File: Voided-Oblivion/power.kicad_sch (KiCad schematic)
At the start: 133 parts, among them Q1 AO3401, Q10 BC847B, Q11 BC847B, Q13 NCE4009S, Q14 NCE4009S, Q2 AO4407A, Q3 BC857, Q4 AO4407A, Q5 AO4407A, Q6 AO4407A, Q7 AO4407A, Q8 BC847B, Q9 BC847B, U10 TLV431BQDBZR, U11 LM2903, U12 AP2171WG-7, U13 TPD2E2U06DRL, U14 TPD2E2U06DRL, U15 LM66100DCKT, U16 AP2171WG-7, U17 LM74700QDDF, U18 LM74700QDDF, U2 TS3USB30ERSWR, U5 TPS54302, U6 TPS54302, U7 TLV76733DRVR, U9 LM66100DCKT

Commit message: pcb almooost done
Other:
- note added: "BS+: Bootstrap rail(5V) PD+: Power Delivery rail (9-20V) +5VA: 5V Analog/clean 5V +5VP: 5V Power/Noisy 5V (for rgb) SM+: Sub-Module power (5V) VBUS: Combined power from both USB-C ports (after ideal diodes)"
- note removed: "BS+: Bootstrap rail(5V) PD+: Power Delivery rail (9-20V) +5VA: 5V Analog/clean 5V +5VP: 5V Power/Noisy 5V (for rgb) SM+: Sub-Module power (5V)"
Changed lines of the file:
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@@
 		)
 	)
-	(text "BS+: Bootstrap rail(5V)\nPD+: Power Delivery rail (9-20V)\n+5VA: 5V Analog/clean 5V\n+5VP: 5V Power/Noisy 5V (for rgb)\nSM+: Sub-Module power (5V)"
+	(text "BS+: Bootstrap rail(5V)\nPD+: Power Delivery rail (9-20V)\n+5VA: 5V Analog/clean 5V\n+5VP: 5V Power/Noisy 5V (for rgb)\nSM+: Sub-Module power (5V)\nVBUS: Combined power from both USB-C ports (after ideal diodes)"
 		(exclude_from_sim no)
 		(at 16.51 274.32 0)

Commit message: THE PCB IS FINAWWYY (electricaly) DONE YAAAAAAAAAAAAAA :33333 ^w^ >w<
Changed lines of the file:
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@@
 	)
 	(junction
+		(at 372.11 157.48)
+		(diameter 0)
+		(color 0 0 0 0)
+	)
+	(junction
 		(at 83.82 77.47)
 		(diameter 0)
@@
 	)
 	(junction
+		(at 251.46 162.56)
+		(diameter 0)
+		(color 0 0 0 0)
+	)
+	(junction
 		(at 88.9 179.07)
 		(diameter 0)
@@
 	)
 	(symbol
+		(lib_id "power:PWR_FLAG")
+		(at 372.11 157.48 270)
+		(unit 1)
+		(body_style 1)
+		(exclude_from_sim no)
+		(in_bom yes)
+		(on_board yes)
+		(in_pos_files yes)
+		(dnp no)
+		(fields_autoplaced yes)
+		(property "Reference" "#FLG012"
+			(at 374.015 157.48 0)
+			(hide yes)
+			(show_name no)
+			(do_not_autoplace no)
+			(effects
+				(font
+					(size 1.27 1.27)
+				)
+			)
+		)
+		(property "Value" "PWR_FLAG"
+			(at 375.92 157.4799 90)
+			(show_name no)
+			(do_not_autoplace no)
+			(effects
+				(font
+					(size 1.27 1.27)
+				)
+				(justify left)
+			)
+		)
+		(property "Footprint" ""
+			(at 372.11 157.48 0)
+			(hide yes)
+			(show_name no)
+			(do_not_autoplace no)
+			(effects
+				(font
+					(size 1.27 1.27)
+				)
+			)
+		)
+		(property "Datasheet" ""
+			(at 372.11 157.48 0)
+			(hide yes)
+			(show_name no)
+			(do_not_autoplace no)
+			(effects
+				(font
+					(size 1.27 1.27)
+				)
+			)
+		)
+		(property "Description" "Special symbol for telling ERC where power comes from"
+			(at 372.11 157.48 0)
+			(hide yes)
+			(show_name no)
+			(do_not_autoplace no)
+			(effects
+				(font
+					(size 1.27 1.27)
+				)
+			)
+		)
+		(pin "1"
+		)
+		(instances
+			(project "Voided-Oblivion"
+				(path "/d39297fe-343b-4cf0-9c31-a16e101c76da/889be6bb-77c0-4884-a2da-d27e1f17090a"
+					(reference "#FLG012")
+					(unit 1)
+				)
+			)
+		)
+	)
+	(symbol
 		(lib_id "Device:R")
 		(at 123.19 246.38 180)
@@
 					(unit 1)
 				)
+			)
+		)
+	)
+	(symbol
+		(lib_id "power:PWR_FLAG")
+		(at 251.46 162.56 90)
+		(unit 1)
+		(body_style 1)
+		(exclude_from_sim no)
+		(in_bom yes)
+		(on_board yes)
+		(in_pos_files yes)
+		(dnp no)
+		(fields_autoplaced yes)
+		(property "Reference" "#FLG011"
+			(at 249.555 162.56 0)
+			(hide yes)
+			(show_name no)
+			(do_not_autoplace no)
+			(effects
+				(font
+					(size 1.27 1.27)
+				)
+			)
+		)
+		(property "Value" "PWR_FLAG"
+			(at 247.65 162.5599 90)
+			(show_name no)
+			(do_not_autoplace no)
+			(effects
+				(font
+					(size 1.27 1.27)
+				)
+				(justify left)
+			)
+		)
+		(property "Footprint" ""
+			(at 251.46 162.56 0)
+			(hide yes)
+			(show_name no)
+			(do_not_autoplace no)
+			(effects
+				(font
+					(size 1.27 1.27)
+				)
+			)
+		)
+		(property "Datasheet" ""
+			(at 251.46 162.56 0)
+			(hide yes)
+			(show_name no)
+			(do_not_autoplace no)
+			(effects
+				(font
+					(size 1.27 1.27)
+				)
+			)
+		)
+		(property "Description" "Special symbol for telling ERC where power comes from"
+			(at 251.46 162.56 0)
+			(hide yes)
+			(show_name no)
+			(do_not_autoplace no)
+			(effects
+				(font
+					(size 1.27 1.27)
+				)
+			)
+		)
+		(pin "1"
+		)
+		(instances
+			(project "Voided-Oblivion"
+				(path "/d39297fe-343b-4cf0-9c31-a16e101c76da/889be6bb-77c0-4884-a2da-d27e1f17090a"
+					(reference "#FLG011")
+					(unit 1)
+				)

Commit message: small changes
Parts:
- C114, C115, C116, C117, C118, C119, C120, C127, C128, C129, C130, C23, C24, C25, C27, C30, C32, C33, C36, C37, C38, C39, C41, C42, C43, C44, C45, C76: footprint Capacitor_SMD:C_0402_1005Metric -> Voided-Oblivion-misc:C_0402_1005Metric-no-silkscreen-text
- R102, R103, R12, R14, R15, R16, R18, R19, R20, R21, R22, R24, R25, R26, R27, R28, R29, R32, R33, R34, R35, R37, R38, R39, R40, R41, R42, R43, R44, R45, R46, R47, R48, R49, R50, R51, R67, R68, R69, R70, R71, R72, R73, R74, R75, R76, R77, R78, R79, R80, R81, R82, R83, R92, R95, R96: footprint Resistor_SMD:R_0402_1005Metric -> Voided-Oblivion-misc:R_0402_1005Metric-no-silkscreen-text
- R30: footprint Resistor_SMD:R_0402_1005Metric -> Voided-Oblivion-misc:R_0402_1005Metric-no-silkscreen-text; MPN ARG02BTC4422 -> ARG02BTC3572
- R31: footprint Resistor_SMD:R_0402_1005Metric -> Voided-Oblivion-misc:R_0402_1005Metric-no-silkscreen-text; MPN (none) -> ARG02BTC1002
- R36: value 10kΩ -> 1kΩ; footprint Resistor_SMD:R_0402_1005Metric -> Voided-Oblivion-misc:R_0402_1005Metric-no-silkscreen-text; LCSC C25744 -> C11702; MPN 0402WGF1002TCE -> 0402WGF1001TCE
- U10: symbol Reference_Voltage:TL431DBZ -> Voided-Oblivion-misc:TL431BQDBZ
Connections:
- net +1V24ref: now also U10.2 (K); no longer U10.1 (K)
- net VBUS1: now also R37.1
- net VBUS2: no longer R37.1
- net at R27.1, R28.2: now also U10.1 (REF); no longer U10.2 (REF)
- net at Q3.3 (C): now also R36.2; no longer R36.1
- net at C45.1, D5.1 (A), Q1.1 (G)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: now also R36.1; no longer R36.2
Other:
- moved on the sheet: C39, D3, R37

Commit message: i think everything but silk is acctualy done this time for reals
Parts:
- R38: value 100kΩ -> 4.7kΩ; LCSC C25741 -> C25900; MPN 0402WGF1003TCE -> 0402WGF4701TCE
- R79, R80, R81, R82: value 100kΩ -> 2.2kΩ; LCSC C25741 -> (none); MPN 0402WGF1003TCE -> (none); Manufacturer UNI-ROYAL(Uniroyal Elec) -> (none)

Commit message: BOMB update  (ignore the "B" on the end of that first word, it has no significant meaning) and some library linking
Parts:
- C121, C40, C77: LCSC C315248 -> C89632; MPN CL05A106MP5NUNC -> CL31B106KBHNNNE
- C26, C31: LCSC (none) -> C89632; MPN (none) -> CL31B106KBHNNNE; Manufacturer (none) -> Samsung Electro-Mechanics
- C28, C29, C34, C35: LCSC (none) -> C12891; MPN (none) -> CL31A226KAHNNNE; Manufacturer (none) -> Samsung Electro-Mechanics
- Q13, Q14: MPN (none) -> NCE4009S; Manufacturer (none) -> Wuxi NCE Power Semiconductor
- R22: MPN (none) -> 0402WGF5101TCE; Manufacturer (none) -> UNI-ROYAL(Uniroyal Elec)
- R31: Manufacturer (none) -> Viking Tech
- R75, R76, R77, R78: value 10kΩ -> 4.7kΩ; LCSC C25744 -> C25900; MPN 0402WGF1002TCE -> 0402WGF4701TCE
- R79, R80, R81, R82: LCSC (none) -> C25879; MPN (none) -> 0402WGF2201TCE; Manufacturer (none) -> UNI-ROYAL(Uniroyal Elec)
- U10: MPN (none) -> TLV431BQDBZR; Manufacturer (none) -> Texas Instruments
- U17, U18: MPN (none) -> LM74700QDDFRQ1; Manufacturer (none) -> Texas Instruments
- USB1, USB2: MPN (none) -> HC-TYPE-C-16P-01A; Manufacturer (none) -> HCTL

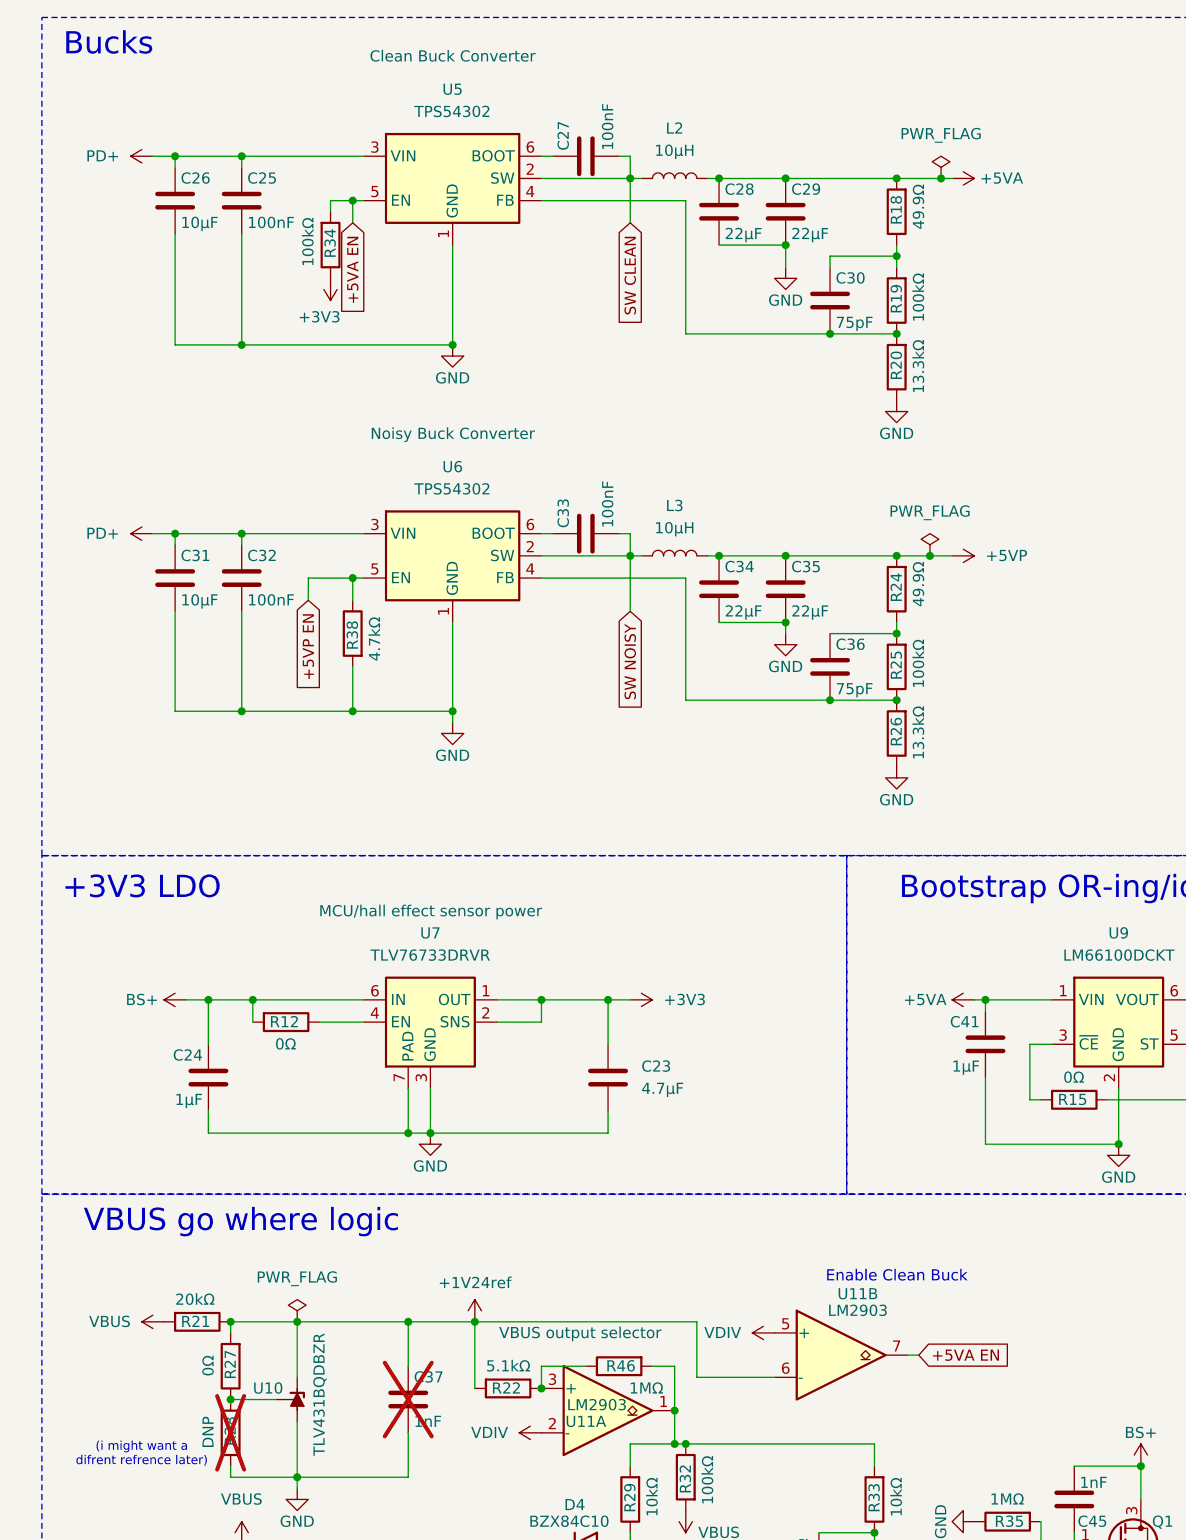
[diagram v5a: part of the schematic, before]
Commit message: change thing to vbus instead of pd
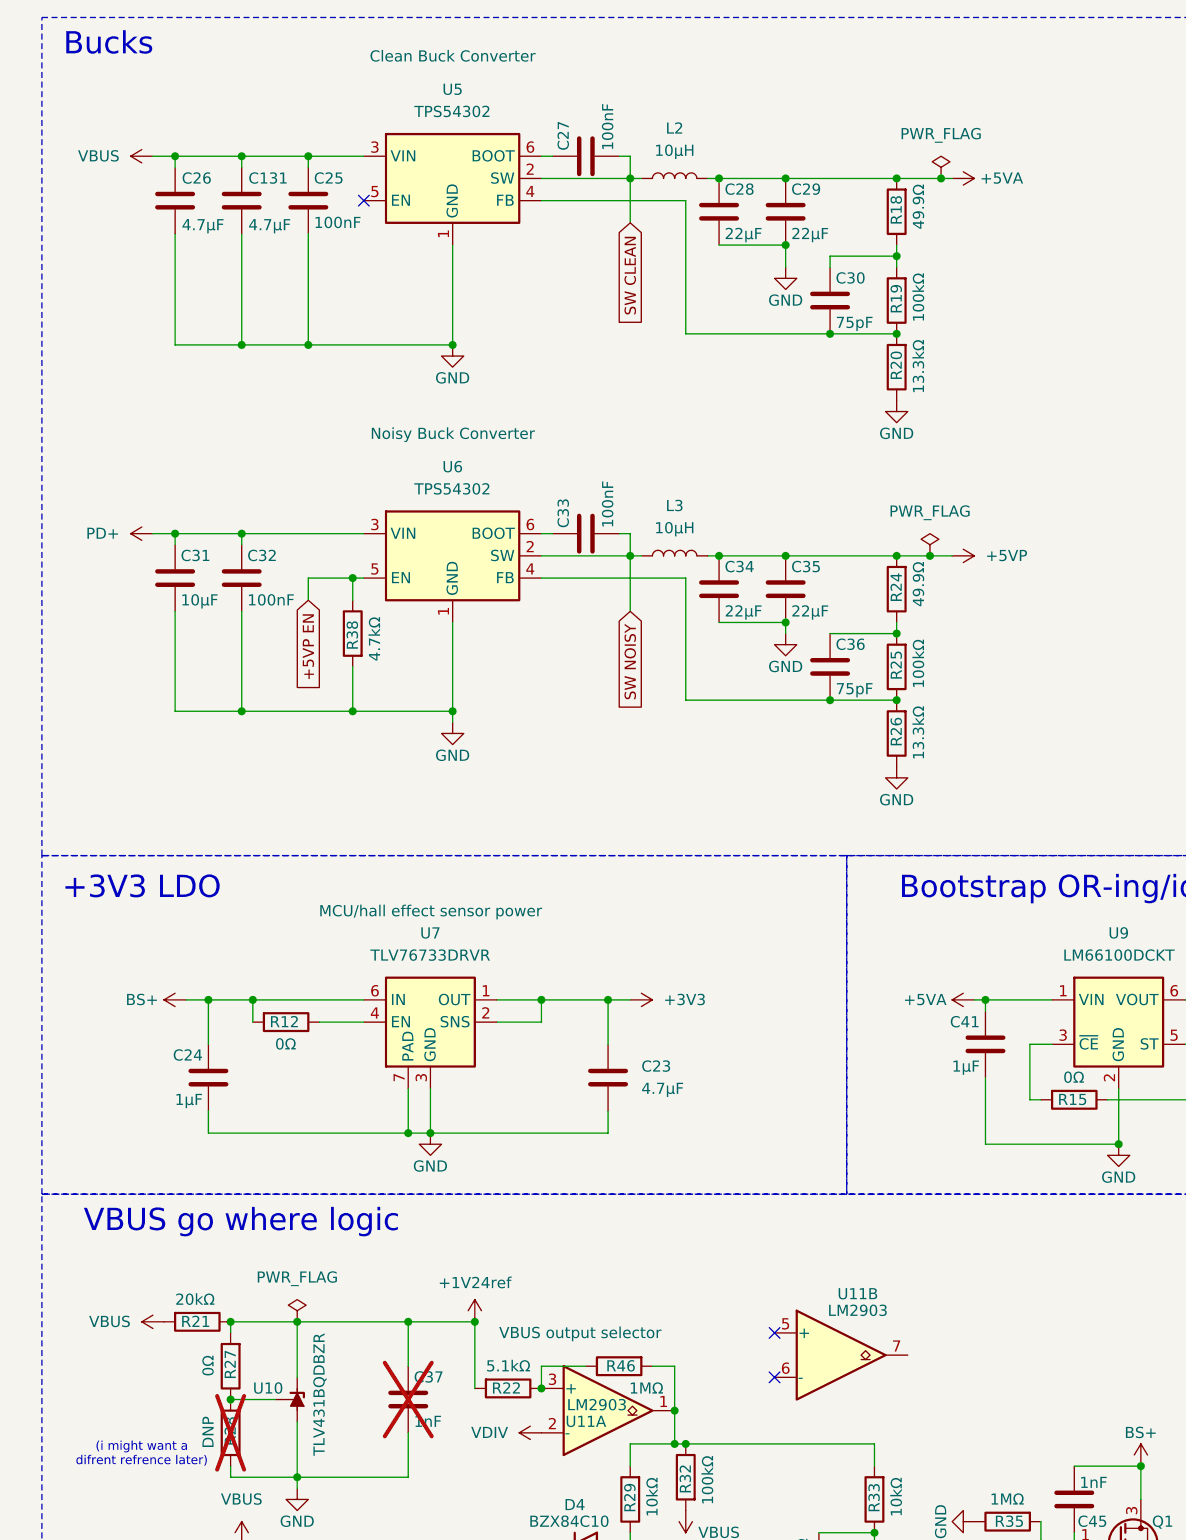
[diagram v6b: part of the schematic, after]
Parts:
- removed R34: 100kΩ, Voided-Oblivion-misc:R_0402_1005Metric-no-silkscreen-text, symbol Device:R
- added C131: 4.7µF, Voided-Oblivion-misc:C_0402_1005Metric-no-silkscreen-text, symbol Device:C
- C26: value 10µF -> 4.7µF; footprint Capacitor_SMD:C_1206_3216Metric -> Voided-Oblivion-misc:C_0402_1005Metric-no-silkscreen-text; LCSC C89632 -> C51205; MPN CL31B106KBHNNNE -> CL31B475KBHNNNE
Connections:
- net +1V24ref: no longer U11.6 (-)
- net GND: now also C131.2
- net PD+: no longer C25.1, C26.1, U5.3 (VIN)
- net VBUS: now also C25.1, C26.1, U5.3 (VIN), C131.1
- net VDIV: no longer U11.5 (+)
- net +5VA EN: no longer names the net of U5.5 (EN)
- net +5VA EN: no longer U11.7
- no-connect marks 14 -> 17
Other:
- note removed: "Enable Clean Buck"
- moved on the sheet: C25

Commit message: UwU
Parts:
- removed TP37: TestPoint, TestPoint:TestPoint_Pad_D1.0mm, symbol Connector:TestPoint
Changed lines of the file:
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@@
 	(wire
 		(pts
-			(xy 309.88 100.33) (xy 309.88 110.49)
-		)
-		(stroke
-			(width 0)
-			(type default)
-		)
-	)
-	(wire
-		(pts
 			(xy 38.1 173.99) (xy 43.18 173.99)
 		)
@@
 		)
 	)
-	(label "SM BUS"
-		(at 309.88 110.49 90)
-		(effects
-			(font
-				(size 1.27 1.27)
-			)
-			(justify left)
-		)
-	)
-	(label "SM BUS"
-		(at 241.3 234.95 0)
-		(effects
-			(font
-				(size 1.27 1.27)
-			)
-			(justify left bottom)
-		)
-	)
 	(global_label "USB1 D-"
 		(shape input)
@@
 		)
 	)
+	(global_label "SM BUS"
+		(shape input)
+		(at 238.76 234.95 90)
+		(fields_autoplaced yes)
+		(effects
+			(font
+				(size 1.27 1.27)
+			)
+			(justify left)
+		)
+		(property "Intersheetrefs" "${INTERSHEET_REFS}"
+			(at 238.76 224.5263 90)
+			(hide yes)
+			(show_name no)
+			(do_not_autoplace no)
+			(effects
+				(font
+					(size 1.27 1.27)
+				)
+				(justify left)
+			)
+		)
+	)
 	(global_label "VBUS2"
 		(shape input)
@@
 					(unit 1)
 				)
-			)
-		)
-	)
-	(symbol
-		(lib_id "Connector:TestPoint")
-		(at 309.88 100.33 0)
-		(unit 1)
-		(body_style 1)
-		(exclude_from_sim no)
-		(in_bom yes)
-		(on_board yes)
-		(in_pos_files yes)
-		(dnp no)
-		(property "Reference" "TP37"
-			(at 309.88 95.25 0)
-			(show_name no)
-			(do_not_autoplace no)
-			(effects
-				(font
-					(size 1.27 1.27)
-				)
-			)
-		)
-		(property "Value" "TestPoint"
-			(at 309.88 97.79 0)
-			(hide yes)
-			(show_name no)
-			(do_not_autoplace no)
-			(effects
-				(font
-					(size 1.27 1.27)
-				)
-			)
-		)
-		(property "Footprint" "TestPoint:TestPoint_Pad_D1.0mm"
-			(at 309.88 100.33 0)
-			(hide yes)
-			(show_name no)
-			(do_not_autoplace no)
-			(effects
-				(font
-					(size 1.27 1.27)
-				)
-			)
-		)
-		(property "Datasheet" "~"
-			(at 309.88 100.33 0)
-			(hide yes)
-			(show_name no)
-			(do_not_autoplace no)
-			(effects
-				(font
-					(size 1.27 1.27)
-				)
-			)
-		)
-		(property "Description" "test point"
-			(at 309.88 100.33 0)
-			(hide yes)
-			(show_name no)
-			(do_not_autoplace no)
-			(effects
-				(font
-					(size 1.27 1.27)
-				)
-			)
-		)
-		(pin "1"
-		)
-		(instances
-			(project "Voided-Oblivion"
-				(path "/d39297fe-343b-4cf0-9c31-a16e101c76da/889be6bb-77c0-4884-a2da-d27e1f17090a"
-					(reference "TP37")
-					(unit 1)
-				)

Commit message: production files i think.com
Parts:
- R28: value DNP -> (none); now left out of the parts list
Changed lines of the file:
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@@
 		(body_style 1)
 		(exclude_from_sim no)
-		(in_bom yes)
+		(in_bom no)
 		(on_board yes)
 		(in_pos_files no)
@@
 			)
 		)
-		(property "Value" "DNP"
+		(property "Value" ""
 			(at 35.56 175.895 90)
 			(show_name no)
@@
 		(in_bom no)
 		(on_board yes)
-		(in_pos_files yes)
+		(in_pos_files no)
 		(dnp yes)
 		(property "Reference" "C37"
